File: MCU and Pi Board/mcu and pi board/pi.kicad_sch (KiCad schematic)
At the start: 1 part, among them J5 Conn_02x20_Odd_Even

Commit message: added some testpoints and some labeling
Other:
- note added: "Pi Header"
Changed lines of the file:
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@@
 	(generator_version "9.0")
 	(paper "A4")
+	(text "Pi Header"
+		(exclude_from_sim no)
+		(at 109.982 40.64 0)
+		(effects
+			(font
+				(size 1.27 1.27)
+			)
+		)
+	)
 	(label "GPIO 2 (SDA)"
 		(at 93.98 38.1 180)

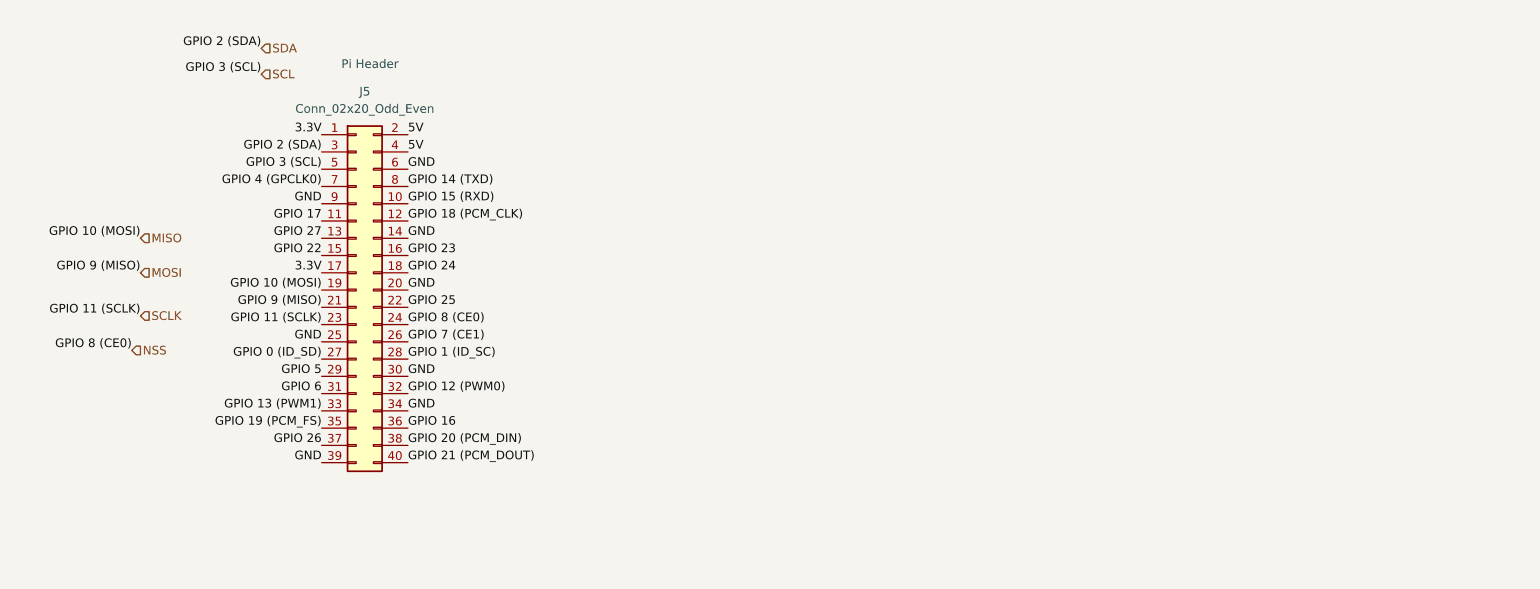
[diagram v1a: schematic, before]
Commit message: added leds and minor fixes
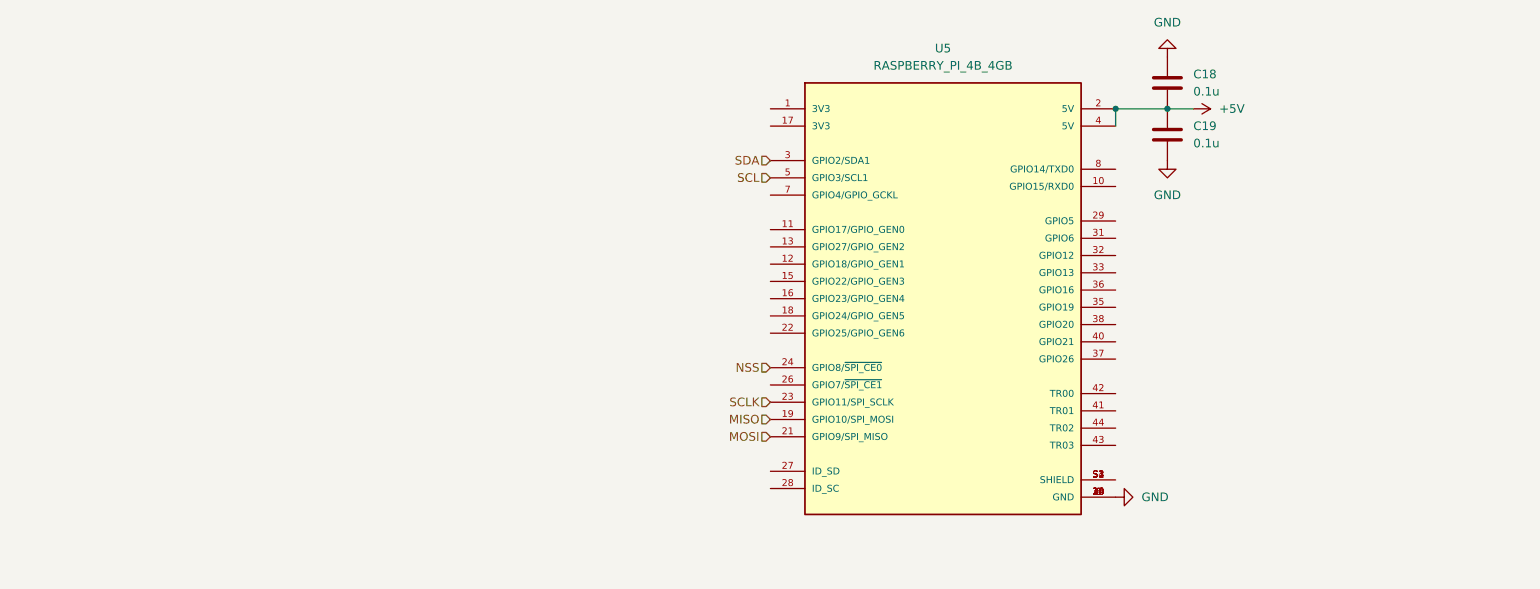
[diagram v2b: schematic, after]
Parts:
- removed J5: Conn_02x20_Odd_Even, symbol Connector_Generic:Conn_02x20_Odd_Even
- added C18, C19: 0.1u, symbol Device:C
- added U5: RASPBERRY_PI_4B_4GB, RASPBERRY_PI_4B_4GB:MODULE_RASPBERRY_PI_4B_4GB, symbol custom library:RASPBERRY_PI_4B_4GB
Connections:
- net GND: now also C18.1, C19.2, U5.14 (GND), U5.20 (GND), U5.25 (GND), U5.30 (GND), U5.34 (GND), U5.39 (GND), U5.6 (GND), U5.9 (GND)
- net MISO: now also U5.19 (GPIO10/SPI_MOSI)
- net MOSI: now also U5.21 (GPIO9/SPI_MISO)
- net NSS: now also U5.24 (GPIO8/~{SPI_CE0})
- net SCL: now also U5.5 (GPIO3/SCL1)
- net SCLK: now also U5.23 (GPIO11/SPI_SCLK)
- net SDA: now also U5.3 (GPIO2/SDA1)
- new net: U5.S1 (SHIELD), U5.S2 (SHIELD), U5.S3 (SHIELD), U5.S4 (SHIELD)
- new net +5V: C18.2, C19.1, U5.2 (5V), U5.4 (5V)
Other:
- note removed: "Pi Header"

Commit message: pretty much done i think
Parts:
- added J12: 430450428, 430450428:MOLEX_430450428, symbol custom library:430450428
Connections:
- net +5V: now also C19.2; no longer C19.1
- net GND: now also C19.1; no longer C19.2
- net MISO: now also U5.21 (GPIO9/SPI_MISO), J12.1; no longer U5.19 (GPIO10/SPI_MOSI)
- net MOSI: now also U5.19 (GPIO10/SPI_MOSI), J12.2; no longer U5.21 (GPIO9/SPI_MISO)
- net SCLK: now also J12.4
- net CS_TOOLS: now reaches U5.26 (GPIO7/~{SPI_CE1})
- net CS_TOOLS: now also J12.3
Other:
- note added: "Tools Board Connector"
- moved on the sheet: C18, C19

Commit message: pretty much done
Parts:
- added J21: Conn_01x28_Socket, symbol Connector:Conn_01x28_Socket
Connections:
- net RP2350B_CS: now reaches U5.37 (GPIO26)
- net NSS renamed STM_CS
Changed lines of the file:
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@@
 		)
 	)
-	(hierarchical_label "NSS"
+	(hierarchical_label "RP2350B_CS"
+		(shape input)
+		(at 219.71 83.82 0)
+		(effects
+			(font
+				(size 1.27 1.27)
+			)
+			(justify left)
+		)
+	)
+	(hierarchical_label "STM_CS"
 		(shape input)
 		(at 168.91 85.09 180)
@@
 					(unit 1)
 				)
+			)
+		)
+	)
+	(symbol
+		(lib_id "Connector:Conn_01x28_Socket")
+		(at 125.73 78.74 180)
+		(unit 1)
+		(exclude_from_sim no)
+		(in_bom yes)
+		(on_board yes)
+		(dnp no)
+		(property "Reference" "J21"
+			(at 128.27 35.306 0)
+			(effects
+				(font
+					(size 1.27 1.27)
+				)
+			)
+		)
+		(property "Value" "Conn_01x28_Socket"
+			(at 128.27 37.846 0)
+			(effects
+				(font
+					(size 1.27 1.27)
+				)
+			)
+		)
+		(property "Footprint" ""
+			(at 125.73 78.74 0)
+			(effects
+				(font
+					(size 1.27 1.27)
+				)
+				(hide yes)
+			)
+		)
+		(property "Datasheet" "~"
+			(at 125.73 78.74 0)
+			(effects
+				(font
+					(size 1.27 1.27)
+				)
+				(hide yes)
+			)
+		)
+		(property "Description" "Generic connector, single row, 01x28, script generated"
+			(at 125.73 78.74 0)
+			(effects
+				(font
+					(size 1.27 1.27)
+				)
+				(hide yes)
+			)
+		)
+		(pin "18"
+		)
+		(pin "20"
+		)
+		(pin "7"
+		)
+		(pin "11"
+		)
+		(pin "9"
+		)
+		(pin "14"
+		)
+		(pin "3"
+		)
+		(pin "4"
+		)
+		(pin "6"
+		)
+		(pin "15"
+		)
+		(pin "13"
+		)
+		(pin "16"
+		)
+		(pin "2"
+		)
+		(pin "8"
+		)
+		(pin "17"
+		)
+		(pin "10"
+		)
+		(pin "5"
+		)
+		(pin "1"
+		)
+		(pin "12"
+		)
+		(pin "19"
+		)
+		(pin "22"
+		)
+		(pin "23"
+		)
+		(pin "24"
+		)
+		(pin "25"
+		)
+		(pin "26"
+		)
+		(pin "21"
+		)
+		(pin "27"
+		)
+		(pin "28"
+		)
+		(instances
+			(project "mcu and pi board"
+				(path "/b20a486a-db1b-4621-abfe-a5d205c676b3/dda479c6-78f4-4e1c-82b6-b799f08d03a6"
+					(reference "J21")
+					(unit 1)
+				)

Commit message: started routing
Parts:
- removed J21: Conn_01x28_Socket, symbol Connector:Conn_01x28_Socket
- added J11: Conn_02x13_Odd_Even, Connector_PinSocket_2.54mm:PinSocket_2x13_P2.54mm_Vertical, symbol Connector_Generic:Conn_02x13_Odd_Even
- C18, C19: footprint (none) -> Capacitor_SMD:C_0603_1608Metric_Pad1.08x0.95mm_HandSolder
- J12: footprint 430450428:MOLEX_430450428 -> custom library:MOLEX_430450428
- U5: footprint RASPBERRY_PI_4B_4GB:MODULE_RASPBERRY_PI_4B_4GB -> custom library:MODULE_RASPBERRY_PI_4B_4GB
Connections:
- net CS_TOOLS: now also J11.23 (Pin_23)
- net GPIO15: now reaches U5.10 (GPIO15/RXD0)
- net GPIO15: now also J11.21 (Pin_21)
- net GPIO17: now reaches U5.11 (GPIO17/GPIO_GEN0)
- net GPIO17: now also J11.8 (Pin_8)
- net GPIO18: now reaches U5.12 (GPIO18/GPIO_GEN1)
- net GPIO18: now also J11.12 (Pin_12)
- net GPIO27: now reaches U5.13 (GPIO27/GPIO_GEN2)
- net GPIO27: now also J11.10 (Pin_10)
- net GPIO22: now reaches U5.15 (GPIO22/GPIO_GEN3)
- net GPIO22: now also J11.14 (Pin_14)
- net GPIO23: now reaches U5.16 (GPIO23/GPIO_GEN4)
- net GPIO23: now also J11.16 (Pin_16)
- net GPIO24: now reaches U5.18 (GPIO24/GPIO_GEN5)
- net GPIO24: now also J11.18 (Pin_18)
- net GPIO25: now reaches U5.22 (GPIO25/GPIO_GEN6)
- net GPIO25: now also J11.20 (Pin_20)
- net ID_SD: now reaches U5.27 (ID_SD)
- net ID_SD: now also J11.2 (Pin_2)
- net ID_SC: now reaches U5.28 (ID_SC)
- net ID_SC: now also J11.4 (Pin_4)
- net GPIO5: now reaches U5.29 (GPIO5)
- net GPIO5: now also J11.3 (Pin_3)
- net GPIO6: now reaches U5.31 (GPIO6)
- net GPIO6: now also J11.5 (Pin_5)
- net GPIO12: now reaches U5.32 (GPIO12)
- net GPIO12: now also J11.7 (Pin_7)
- net GPIO13: now reaches U5.33 (GPIO13)
- net GPIO13: now also J11.9 (Pin_9)
- net GPIO19: now reaches U5.35 (GPIO19)
- net GPIO19: now also J11.13 (Pin_13)
- net GPIO16: now reaches U5.36 (GPIO16)
- net GPIO16: now also J11.11 (Pin_11)
- net GPIO20: now reaches U5.38 (GPIO20)
- net GPIO20: now also J11.15 (Pin_15)
- net GPIO21: now reaches U5.40 (GPIO21)
- net GPIO21: now also J11.17 (Pin_17)
- net TR01: now reaches U5.41 (TR01)
- net TR01: now also J11.24 (Pin_24)
- net TR00: now reaches U5.42 (TR00)
- net TR00: now also J11.22 (Pin_22)
- net TR03: now reaches U5.43 (TR03)
- net TR03: now also J11.1 (Pin_1)
- net TR02: now reaches U5.44 (TR02)
- net TR02: now also J11.26 (Pin_26)
- net GPIO4: now reaches U5.7 (GPIO4/GPIO_GCKL)
- net GPIO4: now also J11.6 (Pin_6)
- net GPIO14: now reaches U5.8 (GPIO14/TXD0)
- net GPIO14: now also J11.19 (Pin_19)
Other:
- moved on the sheet: J12

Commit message: yeet
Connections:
- no-connect marks 0 -> 1
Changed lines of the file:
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@@
 		(color 0 0 0 0)
+	)
+	(no_connect
+		(at 219.71 101.6)
 	)
 	(wire

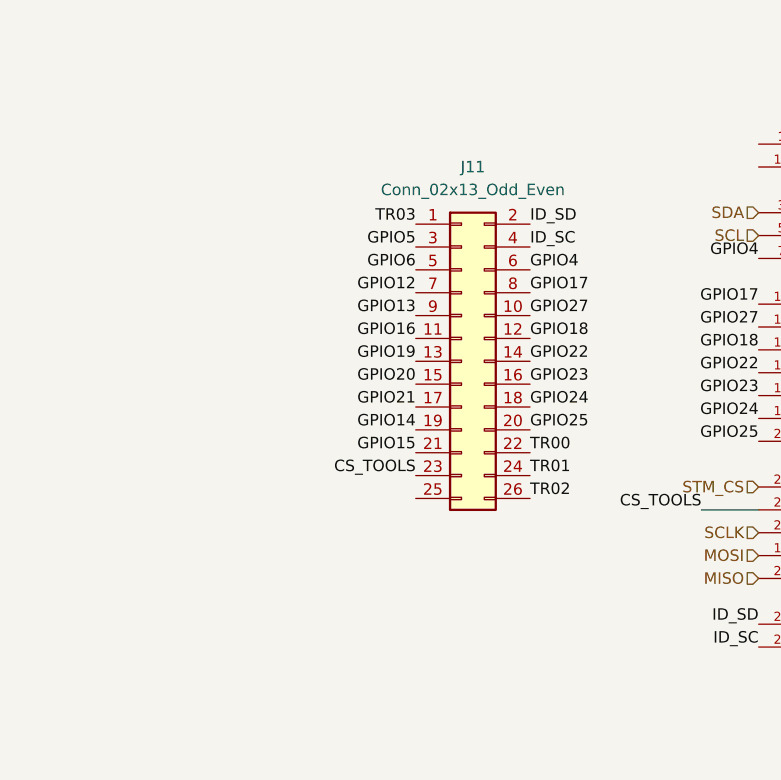
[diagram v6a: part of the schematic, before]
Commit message: split pi connector
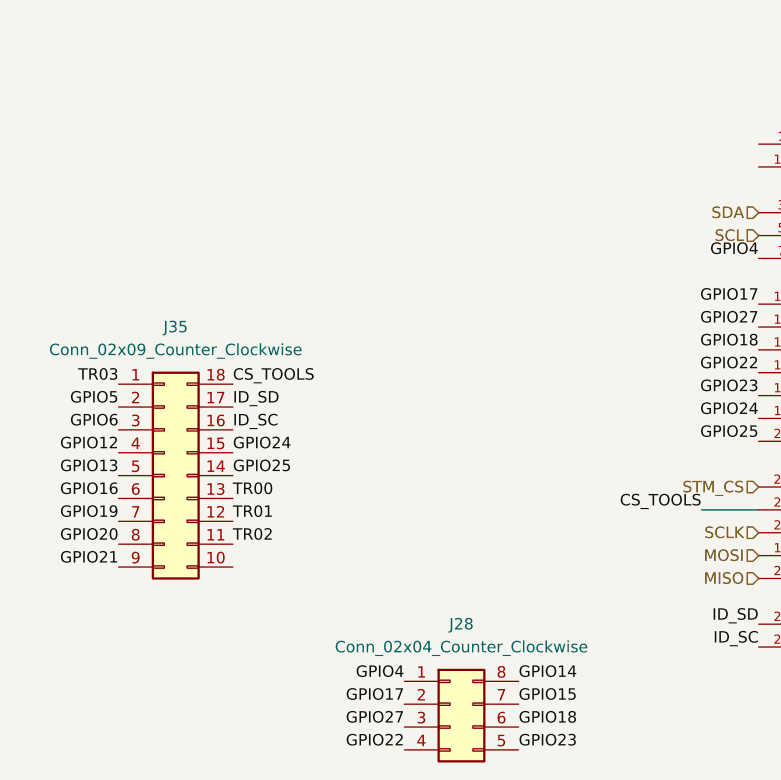
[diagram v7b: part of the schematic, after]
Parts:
- removed J11: Conn_02x13_Odd_Even, Connector_PinSocket_2.54mm:PinSocket_2x13_P2.54mm_Vertical, symbol Connector_Generic:Conn_02x13_Odd_Even
- added J28: Conn_02x04_Counter_Clockwise, Connector_PinHeader_2.54mm:PinHeader_2x04_P2.54mm_Vertical, symbol Connector_Generic:Conn_02x04_Counter_Clockwise
- added J35: Conn_02x09_Counter_Clockwise, Connector_PinHeader_2.54mm:PinHeader_2x09_P2.54mm_Vertical, symbol Connector_Generic:Conn_02x09_Counter_Clockwise
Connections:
- net CS_TOOLS: now also J35.18 (Pin_18)
- net GPIO12: now also J35.4 (Pin_4)
- net GPIO13: now also J35.5 (Pin_5)
- net GPIO14: now also J28.8 (Pin_8)
- net GPIO15: now also J28.7 (Pin_7)
- net GPIO16: now also J35.6 (Pin_6)
- net GPIO17: now also J28.2 (Pin_2)
- net GPIO18: now also J28.6 (Pin_6)
- net GPIO19: now also J35.7 (Pin_7)
- net GPIO20: now also J35.8 (Pin_8)
- net GPIO21: now also J35.9 (Pin_9)
- net GPIO22: now also J28.4 (Pin_4)
- net GPIO23: now also J28.5 (Pin_5)
- net GPIO24: now also J35.15 (Pin_15)
- net GPIO25: now also J35.14 (Pin_14)
- net GPIO27: now also J28.3 (Pin_3)
- net GPIO4: now also J28.1 (Pin_1)
- net GPIO5: now also J35.2 (Pin_2)
- net GPIO6: now also J35.3 (Pin_3)
- net ID_SC: now also J35.16 (Pin_16)
- net ID_SD: now also J35.17 (Pin_17)
- net TR00: now also J35.13 (Pin_13)
- net TR01: now also J35.12 (Pin_12)
- net TR02: now also J35.11 (Pin_11)
- net TR03: now also J35.1 (Pin_1)

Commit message: basically done, added a bunch of vias for no reason, for love of the game
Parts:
- C19: value 0.1u -> 10u
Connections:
- net CS_TOOLS: now also J35.15 (Pin_15); no longer J35.18 (Pin_18)
- net GPIO12: now also J35.12 (Pin_12); no longer J35.4 (Pin_4)
- net GPIO16: now also J35.10 (Pin_10); no longer J35.6 (Pin_6)
- net GPIO21: now also J35.6 (Pin_6); no longer J35.9 (Pin_9)
- net GPIO24: now also J35.18 (Pin_18); no longer J35.15 (Pin_15)
- net GPIO25: now also J35.16 (Pin_16); no longer J35.14 (Pin_14)
- net GPIO5: now also J35.11 (Pin_11); no longer J35.2 (Pin_2)
- net GPIO6: now also J35.9 (Pin_9); no longer J35.3 (Pin_3)
- net ID_SC: now also J35.14 (Pin_14); no longer J35.16 (Pin_16)
- net ID_SD: now also J35.13 (Pin_13); no longer J35.17 (Pin_17)
- net TR00: now also J35.2 (Pin_2); no longer J35.13 (Pin_13)
- net TR01: now also J35.1 (Pin_1); no longer J35.12 (Pin_12)
- net TR02: now also J35.4 (Pin_4); no longer J35.11 (Pin_11)
- net TR03: now also J35.3 (Pin_3); no longer J35.1 (Pin_1)
